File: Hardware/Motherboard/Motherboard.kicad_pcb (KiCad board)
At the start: 2 copper layers, 50.8 x 22.9 mm, 44 parts, among them J2 DEBUG_ARM_SW, J3 MC34739, J4 MC34739, J5 53261-0371, Q1 PMV32UP, T1 TEST_PAD, T2 TEST_PAD, T3 TEST_PAD, T4 TEST_PAD, U1 S9KEAZ64ACLH, U2 LD1117S33CTR, U3 TPS60130PWP, U4 MCP73833, X1 ABM7-12.000MHZ-D2Y-T

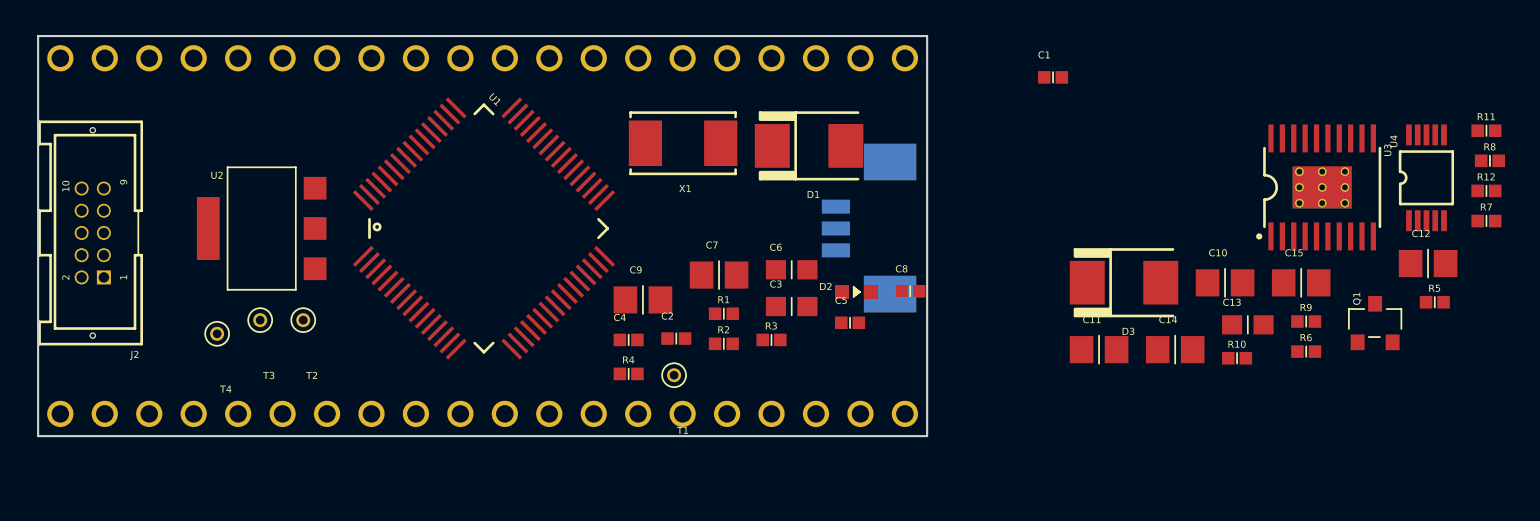
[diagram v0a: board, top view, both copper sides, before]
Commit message: I've layout the motherboard
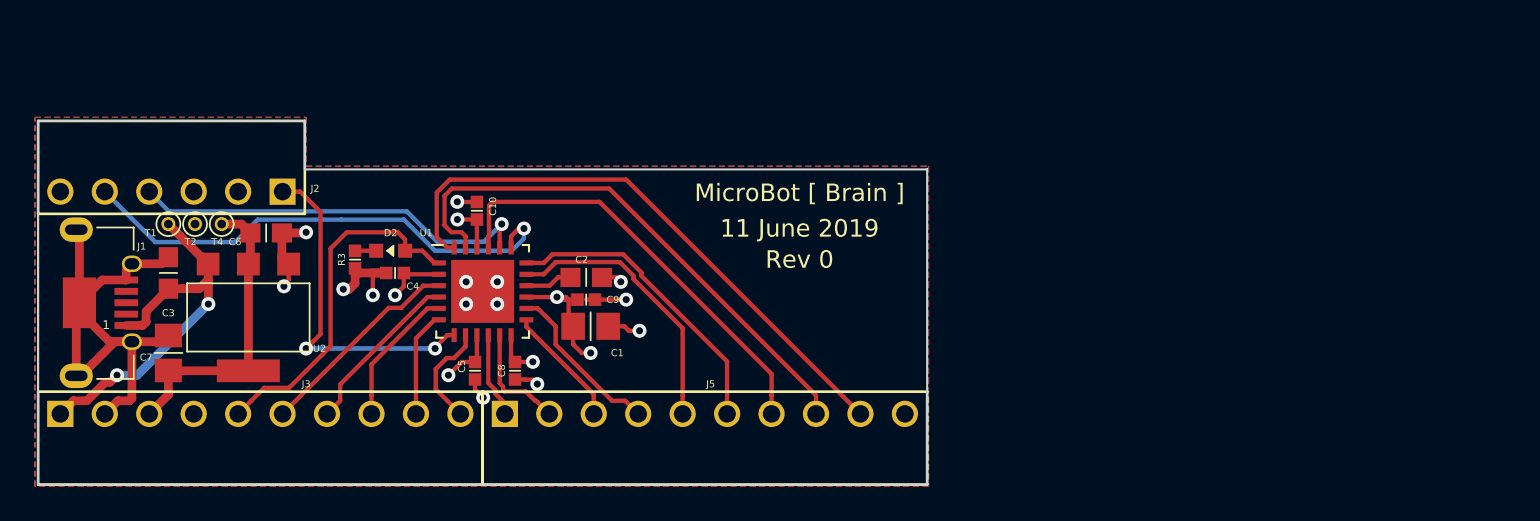
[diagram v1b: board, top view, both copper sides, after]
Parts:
- removed C11: C0805C225K4RACTU, HDE_Capacitors:CAP_0805
- removed C12, C14, C15: C0805C106K8PACTU, HDE_Capacitors:CAP_0805
- removed C13: GRM188R71E105KA12D, HDE_Capacitors:CAP_0603
- removed D1, D3: VS-10BQ030PBF, HDE_Diodes:SMB
- removed J4: MC34739, HDE_Connectors:20pin_1row_2.54mm
- removed Q1: PMV32UP, HDE_IC:SOT23-3
- removed R1: MCMR04X1004FTL, HDE_Resistors:RES_0402
- removed R10, R11, R12, R2, R9: ERJ2RKF2003X, HDE_Resistors:RES_0402
- removed R4: CRCW0402100KFKEDHP, HDE_Resistors:RES_0402
- removed R5: MCWR04X1002FTL, HDE_Resistors:RES_0402
- removed R6: CRCW0402604KFKED, HDE_Resistors:RES_0402
- removed R7: ERJ2RKF4023X, HDE_Resistors:RES_0402
- removed R8: MCMR04X2491FTL, HDE_Resistors:RES_0402
- removed T3: TEST_PAD, HDE_Miscellaneous:TEST_PAD_0.5mm_Hole
- removed U3: TPS60130PWP, HDE_IC:R-PDSO-G20
- removed U4: MCP73833, HDE_IC:MSOP-10
- removed X1: ABM7-12.000MHZ-D2Y-T, HDE_Crystals:ABM7
- added G***: LOGO, HDE_Logo:HDE_Logo_Compact_PCB, B.Cu at (146.1, 90.4)
- added J1: 47590-0001, HDE_Connectors:47590-0001, F.Cu at (102.4, 93.7)
- C1: value MC0402N300J500CT -> C0805C106K8PACTU; footprint HDE_Capacitors:CAP_0402 -> HDE_Capacitors:CAP_0805
- C10: value C0805C225K4RACTU -> C0402C104K4RACAUTO; footprint HDE_Capacitors:CAP_0805 -> HDE_Capacitors:CAP_0402
- C2: value MC0402N300J500CT -> GRM188R71E105KA12D; footprint HDE_Capacitors:CAP_0402 -> HDE_Capacitors:CAP_0603
- C9: value C0805C106K8PACTU -> C0402C104K4RACAUTO; footprint HDE_Capacitors:CAP_0805 -> HDE_Capacitors:CAP_0402
- J2: value DEBUG_ARM_SW -> 61300611021; footprint HDE_Connectors:SHF-105-01-L-D-TH -> HDE_Connectors:6pin_1row_2.54mm_right_angle
- J3: value MC34739 -> 61301011021; footprint HDE_Connectors:20pin_1row_2.54mm -> HDE_Connectors:10pin_1row_2.54mm_right_angle; moved to F.Cu
- J5: value 53261-0371 -> 61301011021; footprint HDE_Connectors:53261-0371 -> HDE_Connectors:10pin_1row_2.54mm_right_angle; moved to F.Cu
- U1: value S9KEAZ64ACLH -> EFM32ZG108F32-QFN24; footprint HDE_IC:LQFP_64 -> HDE_IC:QFN-24_EP_5x5_Pitch0.65mm
- moved C10 42.9 mm to (125.1, 88.4), turned to 90 degrees
- moved C3 35.7 mm to (107.4, 91.9), turned to 90 degrees
- moved C7 31.8 mm to (107.4, 96.5), turned to 90 degrees
- moved T1 30.2 mm to (107.4, 89.2)
- moved C6 30.1 mm to (113.0, 89.7)
- moved C1 30.0 mm to (131.6, 95.0)
- moved D2 26.7 mm to (120.1, 90.7), turned to 180 degrees
- moved R3 24.2 mm to (118.1, 91.2), turned to 270 degrees
- moved J3 24.0 mm to (112.7, 100.0)
- moved C8 23.0 mm to (127.3, 97.5), turned to 270 degrees
- moved C5 21.6 mm to (125.0, 97.5), turned to 270 degrees
- moved J5 14.9 mm to (138.1, 100.0), turned to 0 degrees
- moved C4 13.9 mm to (120.4, 91.9), turned to 180 degrees
- moved T2 8.27 mm to (109.0, 89.2)
- moved T4 6.28 mm to (110.5, 89.2)
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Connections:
- C1 pad 1: /Micro_EXTAL -> +3V3
- C10 pad 1: /Battery Circuit/TPS_C1+ -> +3V3
- C10 pad 2: /Battery Circuit/TPS_C1- -> GND
- C3 pad 1: +5V_Selection -> +5V
- D2 pad 1: /Micro_LED1 -> /Micro_P1_LED1
- J2 pad 1: +3V3 -> /Micro_~RESET~
- J2 pad 2: /Micro_SWDIO -> +3V3
- J2 pad 4: /Micro_SWCLK -> /Micro_SWDIO
- J2 pad 5: GND -> /Micro_SWCLK
- J3 pad 10: (no net) -> /Micro_P6
- J3 pad 3: (no net) -> +3V3
- J3 pad 4: (no net) -> GND
- J3 pad 5: (no net) -> /Micro_P1_LED1
- J3 pad 6: (no net) -> /Micro_P2
- J3 pad 7: (no net) -> /Micro_P3
- J3 pad 8: (no net) -> /Micro_P4
- J3 pad 9: (no net) -> /Micro_P5
- J5 pad 1: (no net) -> /Micro_P7
- J5 pad 2: (no net) -> /Micro_P8
- J5 pad 3: (no net) -> /Micro_P9
- J5 pad 4: (no net) -> /Micro_P10
- T1 pad 1: +3V3 -> +5V
- T2 pad 1: /Micro_~RESET~ -> GND
- T4 pad 1: GND -> +3V3
- U1 pad 1: (no net) -> /Micro_P1_LED1
- U1 pad 10: Net-(U1-Pad10) -> /Micro_P7
- U1 pad 11: /Micro_EXTAL -> /Micro_P8
- U1 pad 12: /Micro_XTAL -> +3V3
- U1 pad 13: (no net) -> /Micro_P9
- U1 pad 14: (no net) -> /Micro_P10
- U1 pad 15: (no net) -> +3V3
- U1 pad 16: (no net) -> Net-(C2-Pad1)
- U1 pad 17: (no net) -> /Micro_P11
- U1 pad 18: (no net) -> /Micro_P12
- U1 pad 19: (no net) -> /Micro_SWCLK
- U1 pad 2: (no net) -> +3V3
- U1 pad 20: (no net) -> /Micro_SWDIO
- U1 pad 21: (no net) -> /Micro_P13
- U1 pad 22: (no net) -> +3V3
- U1 pad 23: (no net) -> /Micro_P14
- U1 pad 24: (no net) -> /Micro_P15
- U1 pad 25: (no net) -> GND
- U1 pad 3: (no net) -> /Micro_P2
- U1 pad 4: (no net) -> /Micro_P3
- U1 pad 5: (no net) -> /Micro_P4
- U1 pad 6: (no net) -> /Micro_P5
- U1 pad 7: +3V3 -> /Micro_~RESET~
- U1 pad 8: +3V3 -> /Micro_P6
- U1 pad 9: Net-(U1-Pad10) -> +3V3
- U2 pad 3: +5V_Selection -> +5V
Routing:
- net GND: track 0.00 -> 50.8 mm, vias 0 -> 14
- net +3V3: track 0.00 -> 37.1 mm, vias 0 -> 6
- net /Micro_P15: track 0.00 -> 33.9 mm
- net /Micro_P14: track 0.00 -> 31.2 mm
- net /Micro_SWCLK: track 0.00 -> 28.8 mm, vias 0 -> 1
- net /Micro_P13: track 0.00 -> 25.0 mm
- net +5V: track 0.00 -> 23.6 mm, vias 0 -> 2
- net /Micro_SWDIO: track 0.00 -> 23.1 mm, vias 0 -> 1
- net /Micro_P1_LED1: track 0.00 -> 20.1 mm
- net /Micro_~RESET~: track 0.00 -> 19.6 mm, vias 0 -> 2
- net /Micro_P12: track 0.00 -> 17.3 mm
- net /Micro_P11: track 0.00 -> 15.8 mm
- net /Micro_P2: track 0.00 -> 12.0 mm
- net /Micro_P3: track 0.00 -> 9.70 mm
- net /Micro_P10: track 0.00 -> 9.49 mm
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- added copper zone on Power, net +3V3
- added copper zone on B.Cu, net GND
- added copper zone on F.Cu, net GND
- added copper zone on Ground, net GND
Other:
- board size 50.8 x 22.9 mm -> 50.8 x 20.8 mm
- copper layers 2 -> 4
- board text added: "11 June 2019"
- board text added: "13"
- board text added: "3.3V"
- board text added: "8"
- board text added: "GND"
- board text added: "MicroBot [ Brain ]"
- board text added: "P1"
- board text added: "P10"
- board text added: "P11"
- board text added: "P12"
- board text added: "P14"
- board text added: "P15"
- board text added: "P2"
- board text added: "P3"
- board text added: "P4"
- board text added: "P5"
- board text added: "P6"
- board text added: "P7"
- board text added: "P9"
- board text added: "Rev 0"
- board text added: "SWD"
- board text added: "Vin"
